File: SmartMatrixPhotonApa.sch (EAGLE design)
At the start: 13 parts, among them IC2 74AHC1G08DBV, IC3 74AHC1G08DBV, J1 0-DNP, U1 microSD

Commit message: Rough routing of board, not close to passing DRC
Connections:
- net V3.3 renamed 3V3
- new net N$1: JP3.GND@2
- net GND: now also JP3.GND@21; no longer JP3.GND@2
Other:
- note added: "Pixelmatix 2016 CC BY-SA 4.0"
- note added: "what if there's no power on VEXT, will it hurt the buffers to drive them with 3.3V?"
- note removed: "Pixelmatix 2016 CC BY-SA"
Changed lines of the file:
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@@
 <part name="J1" library="rcl" deviceset="R-US_" device="R0603" value="0-DNP"/>
 <part name="JP3" library="eclibrary" deviceset="PARTICLE_PHOTON_TEMPLATES" device="_PIXELMATIX" value="PARTICLE_PHOTON_TEMPLATES_PIXELMATIX"/>
-<part name="GND2" library="supply1" deviceset="GND" device=""/>
 <part name="FRAME1" library="frames" deviceset="LETTER_L" device=""/>
+<part name="GND1" library="supply1" deviceset="GND" device=""/>
 </parts>
 <sheets>
@@
 <text x="152.4" y="93.98" size="1.778" layer="94">Optionally add jumper to JP8/JP6 to power strip through VUSB</text>
 <text x="152.4" y="91.44" size="1.778" layer="94">C2 may be unnecessary, will test</text>
-<text x="121.92" y="30.48" size="1.778" layer="91">add a SMT jumper so
+<text x="121.92" y="27.94" size="1.778" layer="91">add a SMT jumper so
 0-ohm resistor isn't needed
 if populated?</text>
 <text x="170.18" y="-15.24" size="3.175" layer="94">SmartMatrix APA102 Shield for Photon</text>
-<text x="170.18" y="-20.32" size="3.048" layer="94">Pixelmatix 2016 CC BY-SA</text>
+<text x="170.18" y="-20.32" size="3.048" layer="94">Pixelmatix 2016 CC BY-SA 4.0</text>
 <text x="256.54" y="-38.1" size="3.048" layer="94">V3</text>
 <text x="68.58" y="129.54" size="3.556" layer="94">Photon</text>
@@
 <text x="187.96" y="60.96" size="3.556" layer="94">APA102 Buffers</text>
 <text x="53.34" y="43.18" size="3.556" layer="94">microSD Card</text>
+<text x="121.92" y="40.64" size="1.778" layer="91">what if there's no power on VEXT,
+will it hurt the buffers to drive
+them with 3.3V?</text>
 </plain>
 <instances>
@@
 <instance part="J1" gate="G$1" x="170.18" y="20.32"/>
 <instance part="JP3" gate="G$1" x="78.74" y="104.14"/>
-<instance part="GND2" gate="1" x="48.26" y="86.36"/>
 <instance part="FRAME1" gate="G$1" x="20.32" y="-45.72"/>
 <instance part="FRAME1" gate="G$2" x="167.64" y="-45.72"/>
+<instance part="GND1" gate="1" x="106.68" y="81.28"/>
 </instances>
 <busses>
@@
 </segment>
 </net>
-<net name="V3.3" class="0">
+<net name="3V3" class="0">
 <segment>
 <wire x1="83.82" y1="27.94" x2="68.58" y2="27.94" width="0.1524" layer="91"/>
@@
 </segment>
 <segment>
-<wire x1="48.26" y1="88.9" x2="48.26" y2="116.84" width="0.1524" layer="91"/>
-<wire x1="48.26" y1="116.84" x2="55.88" y2="116.84" width="0.1524" layer="91"/>
-<pinref part="GND2" gate="1" pin="GND"/>
-<pinref part="JP3" gate="G$1" pin="GND@2"/>
+<pinref part="JP3" gate="G$1" pin="GND@21"/>
+<wire x1="106.68" y1="83.82" x2="106.68" y2="111.76" width="0.1524" layer="91"/>
+<wire x1="106.68" y1="111.76" x2="99.06" y2="111.76" width="0.1524" layer="91"/>
+<pinref part="GND1" gate="1" pin="GND"/>
 </segment>
 </net>
@@
 </segment>
 </net>
+<net name="N$1" class="0">
+<segment>
+<wire x1="48.26" y1="116.84" x2="55.88" y2="116.84" width="0.1524" layer="91"/>
+<pinref part="JP3" gate="G$1" pin="GND@2"/>
+</segment>
+</net>

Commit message: Rev V0.1, ready to order prototypes
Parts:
- added D2: MBR0520LT, diode:MBR0520LT
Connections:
- net N$2 renamed CLK
- net N$3 renamed DAT
- removed net N$1: JP3.GND@2
- net VEXT: now also D2.C
- net VIN: now also D2.A
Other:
- note added: "Optionally add jumper to JP8/JP6 or place diode at D2 to power strip through VUSB"
- note added: "V0.1"
- note removed: "Optionally add jumper to JP8/JP6 to power strip through VUSB"
- note removed: "V3"
- note removed: "add a SMT jumper so 0-ohm resistor isn't needed if populated?"
- note removed: "what if there's no power on VEXT, will it hurt the buffers to drive them with 3.3V?"
- moved on the sheet: C1, IC2, IC2P, IC3P, J1, R1, R2

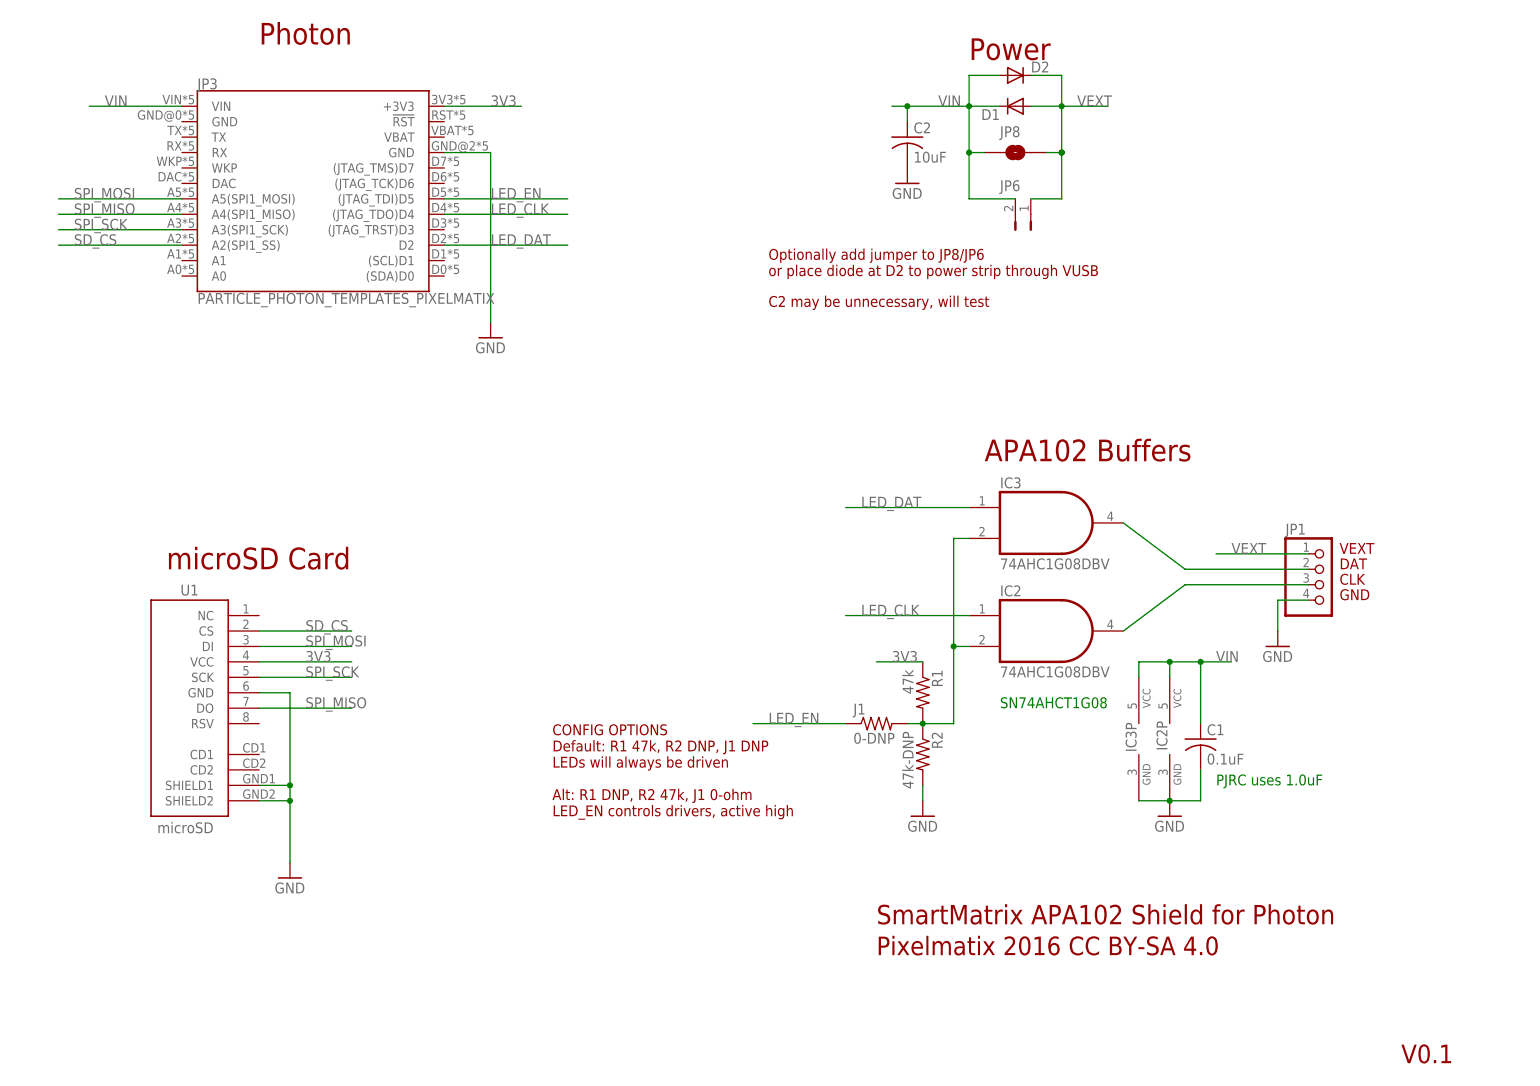
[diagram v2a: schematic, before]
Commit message: Changes for V1 - Larger holes for APA102 wires - a 1x2 SMT jumper on bottom side of board for VIN and VEXT - optional (DNP) 6.3V 100uF smd 1206 cap to shield to help with USB power kickback when long strip switches - fatter VIN/VEXT to support USB power - photon dual header footprint improvements 	- Make it two parts as the connectors are two separate 2x12 headers 	- Fix the unnecessary DRC errors that show up in Eagle - change to shorter 2x12 connectors - update BOM - label pins used for microSD and apa - Put name on bottom of board (top is covered with Photon)
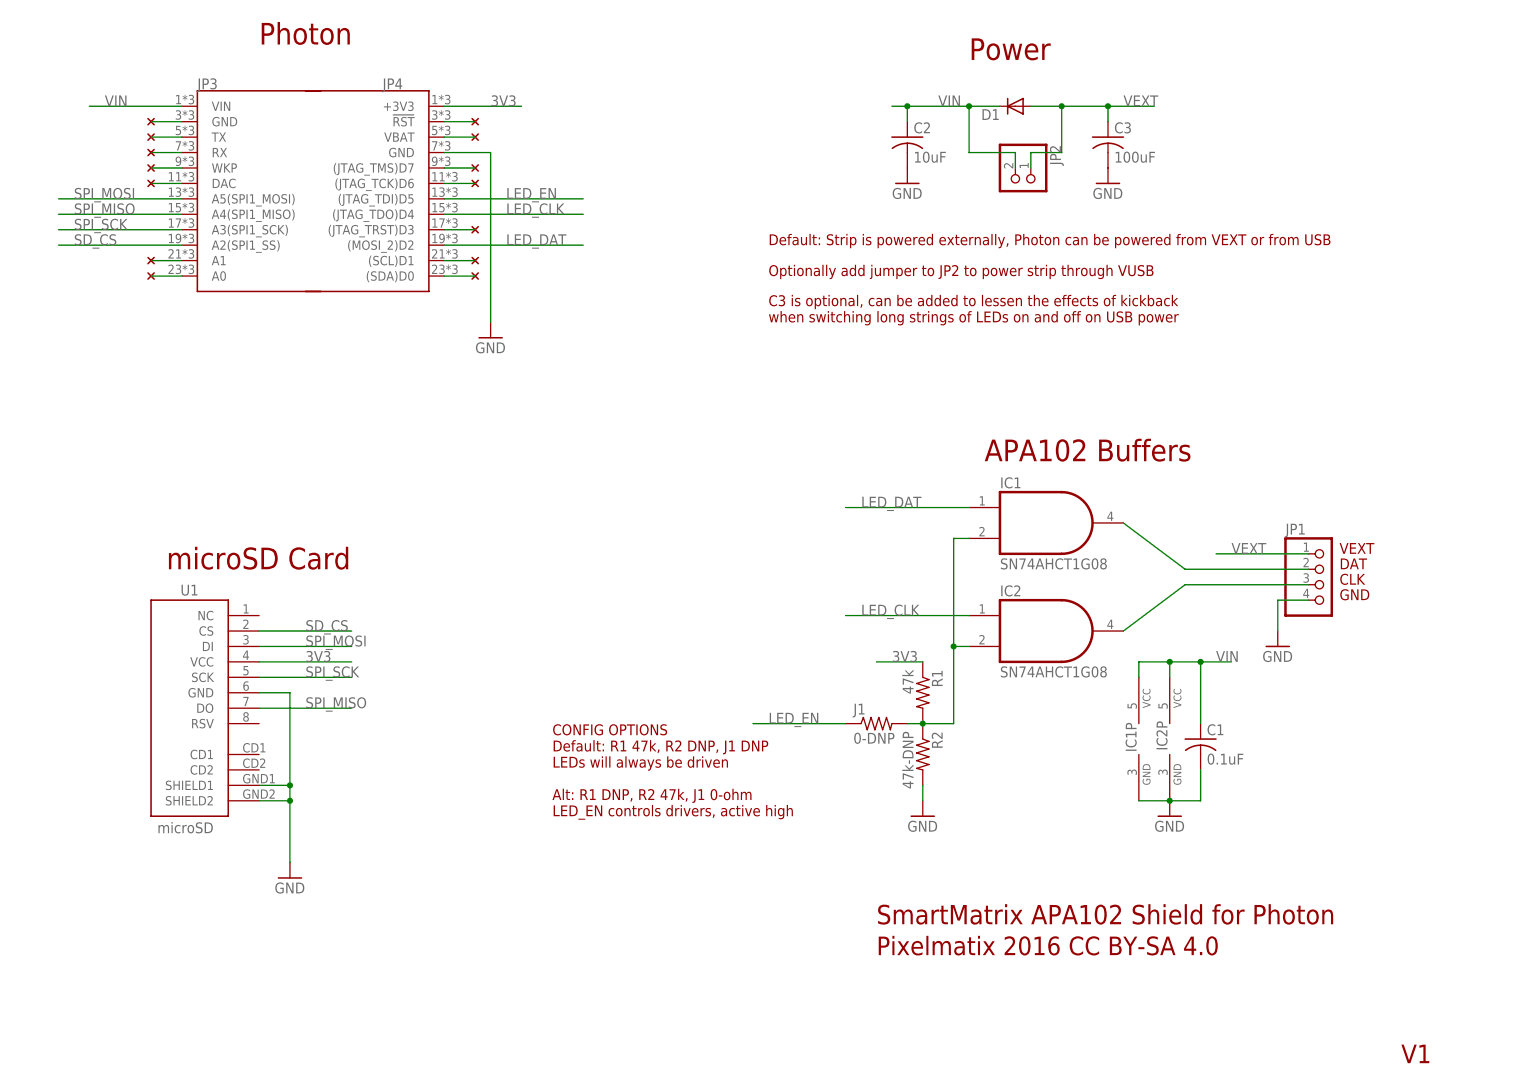
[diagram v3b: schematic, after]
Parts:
- removed D2: MBR0520LT, diode:MBR0520LT
- removed JP6: JUMPER-PTH-2-NO, SparkFun-Passives:JUMPER-PTH-2-NO
- removed JP8: JUMPER-PAD-2-NO, SparkFun-Passives:JUMPER-PAD-2-NO
- added C3: 100uF, scanlime:C-USC1206
- added JP2: (no value), pinhead-2:PINHD-1X02_2.54-SMD-90°
- added JP4: 2x12 Female SMT Socket, eclibrary:PARTICLE_PHOTON_RIGHT_SHIELD_BOT_MOUNT
- added U$1, U$10, U$11, U$12, U$13, U$14, U$2, U$3, U$4, U$5, U$6, U$7, U$8, U$9: NC, eclibrary:NC
- JP1: device pinhead-2:PINHD-1X04_2.54 -> eclibrary:PINHD-1X04_2.54LARGE
- JP3: value PARTICLE_PHOTON_TEMPLATES_PIXELMATIX -> 2x12 Female SMT Socket; device eclibrary:PARTICLE_PHOTON_TEMPLATES_PIXELMATIX -> eclibrary:PARTICLE_PHOTON_LEFT_SHIELD_BOT_MOUNT
- renumbered IC3 to IC1
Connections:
- new net N$1: JP3.GND@2, U$1.P$1
- new net N$10: JP4.VBAT, U$8.P$1
- new net N$11: JP4.(JTAG_TMS)D7, U$9.P$1
- new net N$12: JP4.(JTAG_TCK)D6, U$10.P$1
- new net N$13: JP4.(JTAG_TRST)D3, U$11.P$1
- new net N$14: JP4.(SCL)D1, U$12.P$1
- new net N$15: JP4.(SDA)D0, U$13.P$1
- new net N$2: JP3.TX, U$2.P$1
- new net N$3: JP3.RX, U$3.P$1
- new net N$5: JP3.WKP, U$4.P$1
- new net N$6: JP3.DAC, U$14.P$1
- new net N$7: JP3.A1, U$5.P$1
- new net N$8: JP3.A0, U$6.P$1
- new net N$9: JP4.!RST!, U$7.P$1
- net 3V3: now also JP4.+3V3; no longer JP3.+3V3
- net GND: now also C3.2, JP4.GND@1; no longer JP3.GND@21
- net LED_CLK: now also JP4.(JTAG_TDO)D4; no longer JP3.(JTAG_TDO)D4
- net LED_DAT: now also JP4.(MOSI_2)D2; no longer JP3.D2
- net LED_EN: now also JP4.(JTAG_TDI)D5; no longer JP3.(JTAG_TDI)D5
- net VEXT: now also C3.1, JP2.1; no longer D2.C, JP6.1, JP8.2
- net VIN: now also JP2.2; no longer D2.A, JP6.2, JP8.1
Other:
- note added: "C3 is optional, can be added to lessen the effects of kickback when switching long strings of LEDs on and off on USB power"
- note added: "Default: Strip is powered externally, Photon can be powered from VEXT or from USB"
- note added: "Optionally add jumper to JP2 to power strip through VUSB"
- note added: "V1"
- note removed: "C2 may be unnecessary, will test"
- note removed: "Optionally add jumper to JP8/JP6 or place diode at D2 to power strip through VUSB"
- note removed: "PJRC uses 1.0uF"
- note removed: "V0.1"
